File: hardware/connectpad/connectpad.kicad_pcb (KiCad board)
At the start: 2 copper layers, 50 x 35 mm, 3 parts, among them J1 Conn_01x01, J2 Conn_01x01, J3 Conn_01x01

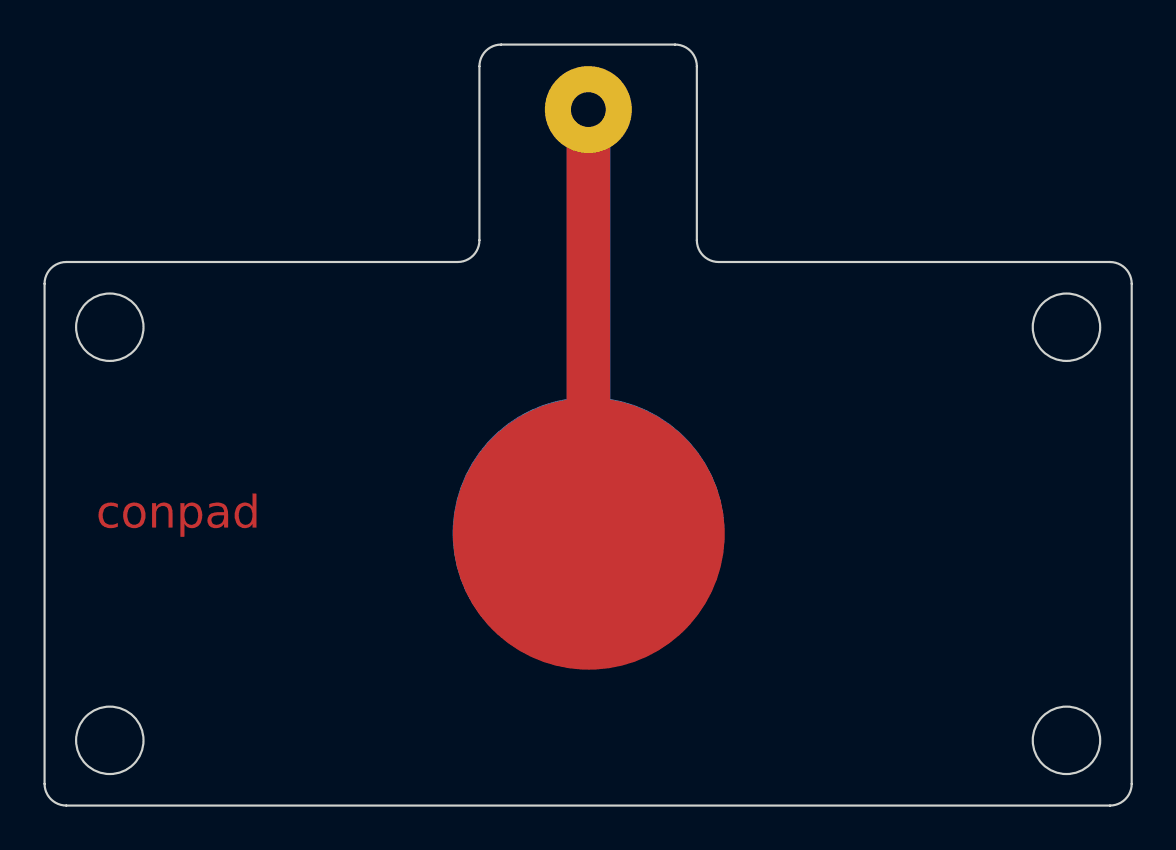
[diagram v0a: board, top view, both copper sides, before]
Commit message: 加入隔热槽设计
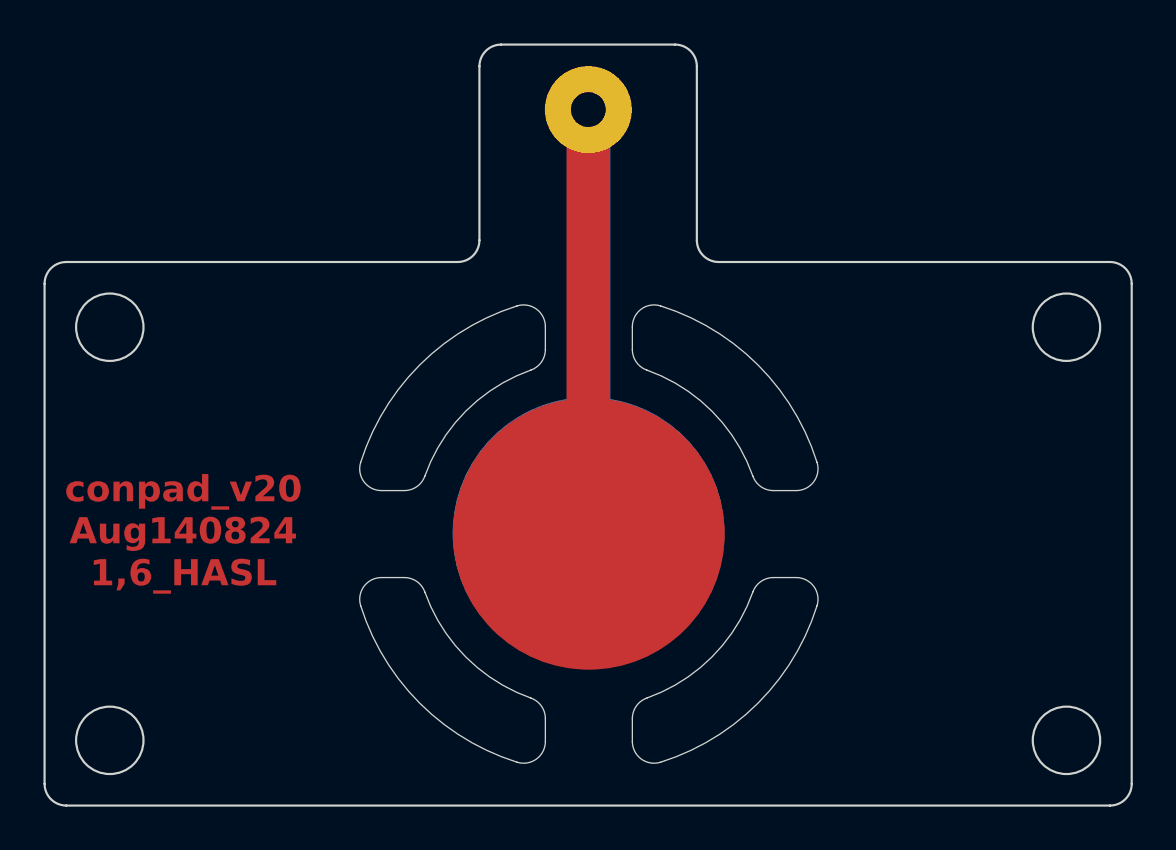
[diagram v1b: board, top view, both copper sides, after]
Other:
- outline, holes or cut-outs redrawn
- net class Default removed
- board text added: "conpad_v20 Aug140824 1,6_HASL"
- board text removed: "conpad"

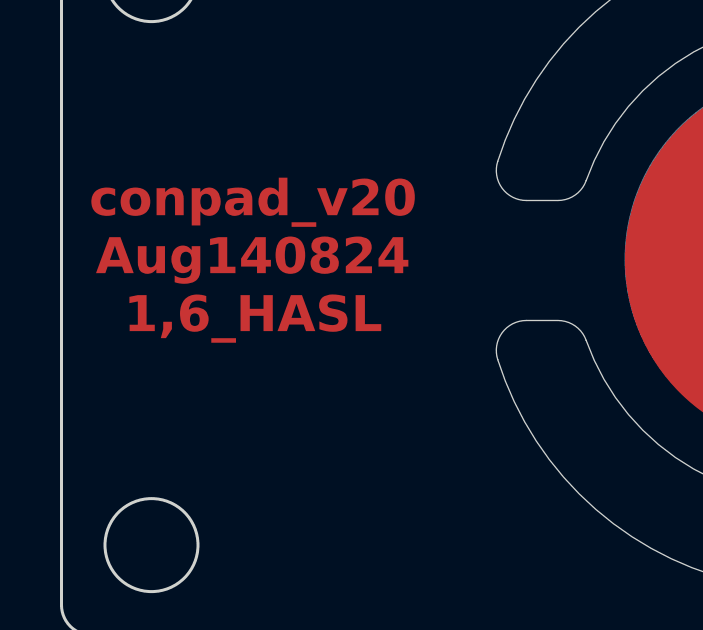
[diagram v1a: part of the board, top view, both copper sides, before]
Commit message: 修改为沉金板
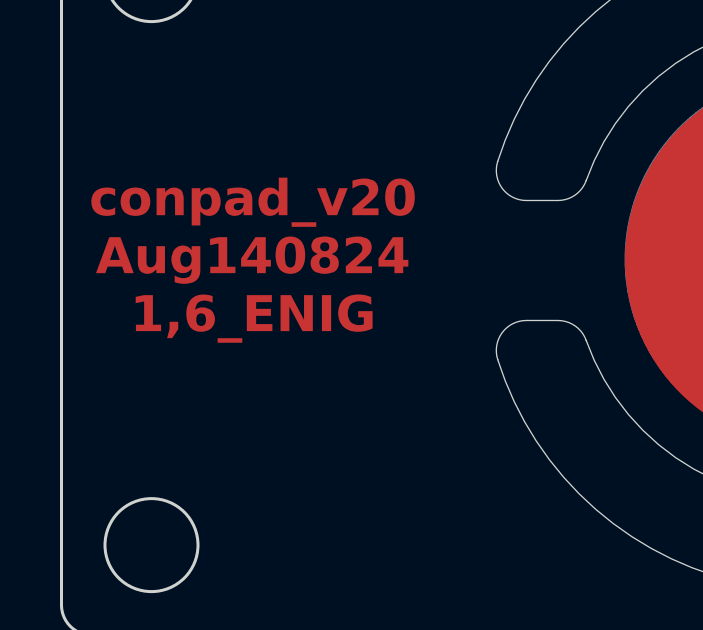
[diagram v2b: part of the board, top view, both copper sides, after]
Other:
- board text added: "conpad_v20 Aug140824 1,6_ENIG"
- board text removed: "conpad_v20 Aug140824 1,6_HASL"
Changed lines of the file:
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@@
   (gr_line (start 131.283145 117.578427) (end 131.283145 118.632538)
     (stroke (width 0.01) (type solid)) (layer "Edge.Cuts"))
-  (gr_text "conpad_v20\nAug140824\n1,6_HASL" (at 110.64 108.96) (layer "F.Cu")
+  (gr_text "conpad_v20\nAug140824\n1,6_ENIG" (at 110.64 108.96) (layer "F.Cu")
     (effects (font (size 1.2 1.2) (thickness 0.2) bold))
   )
